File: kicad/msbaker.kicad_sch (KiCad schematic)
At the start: 32 parts

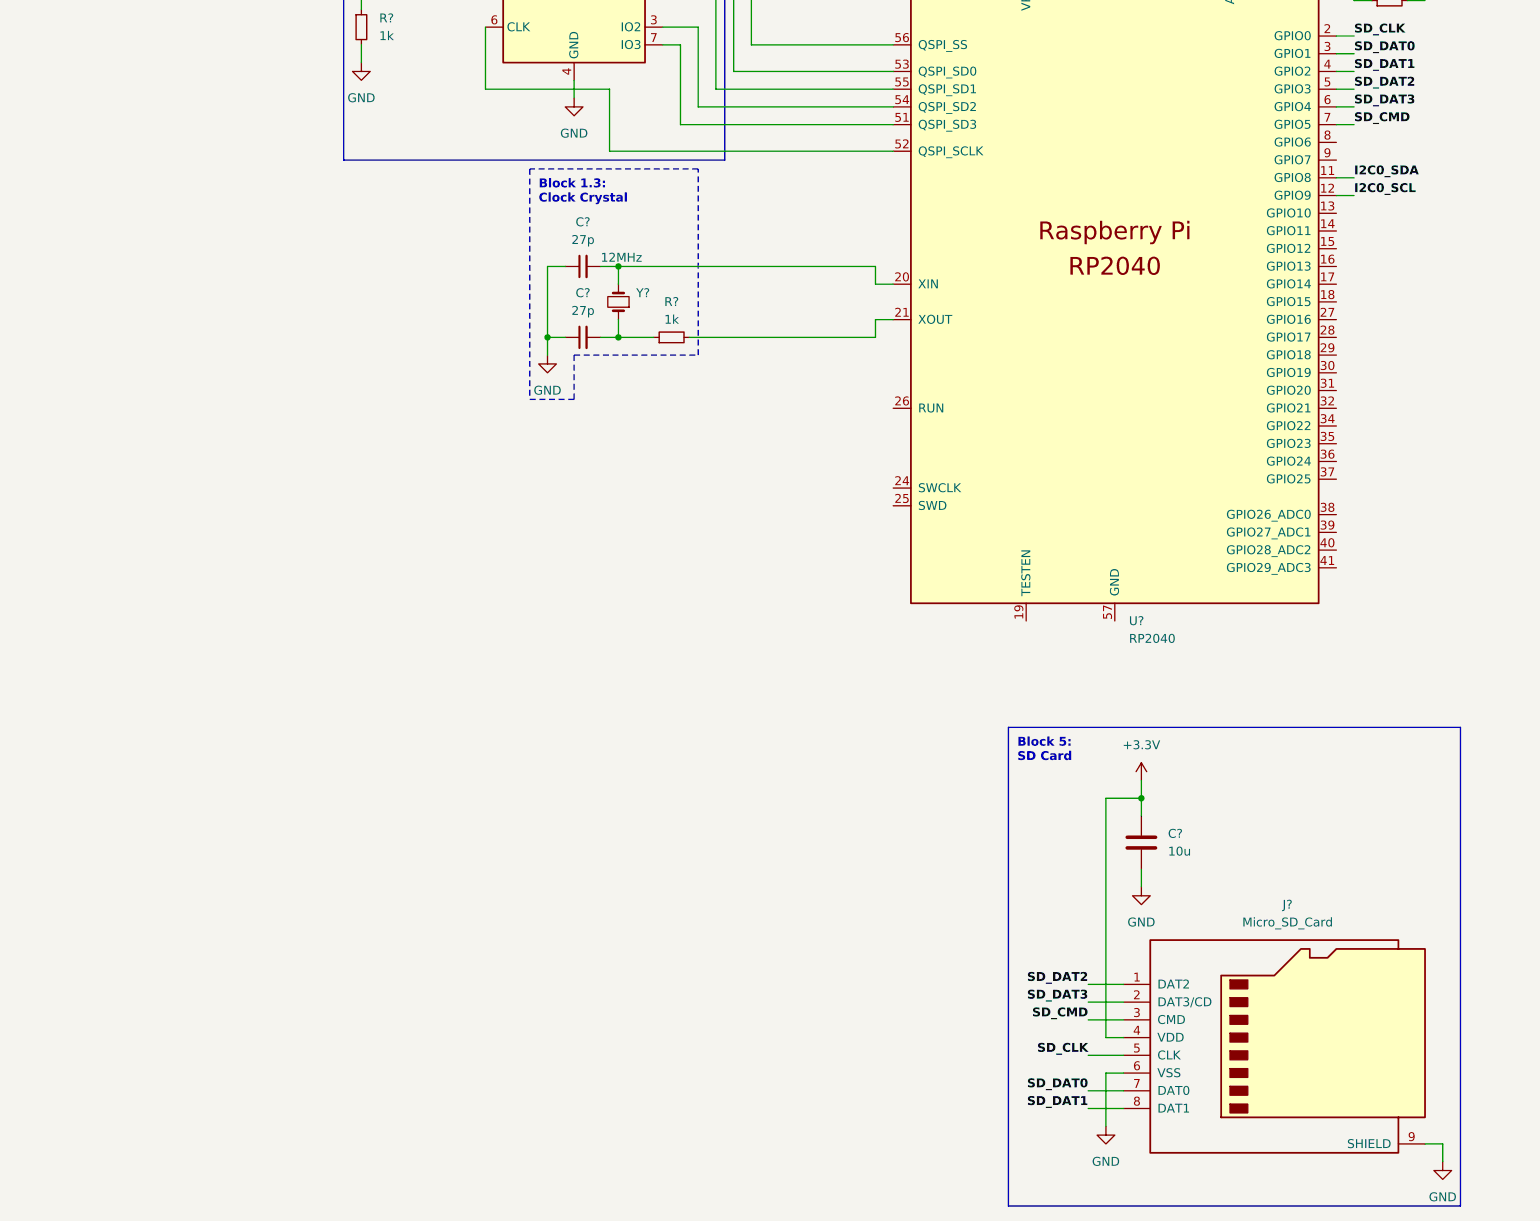
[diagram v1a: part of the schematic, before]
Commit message: Added gpio block
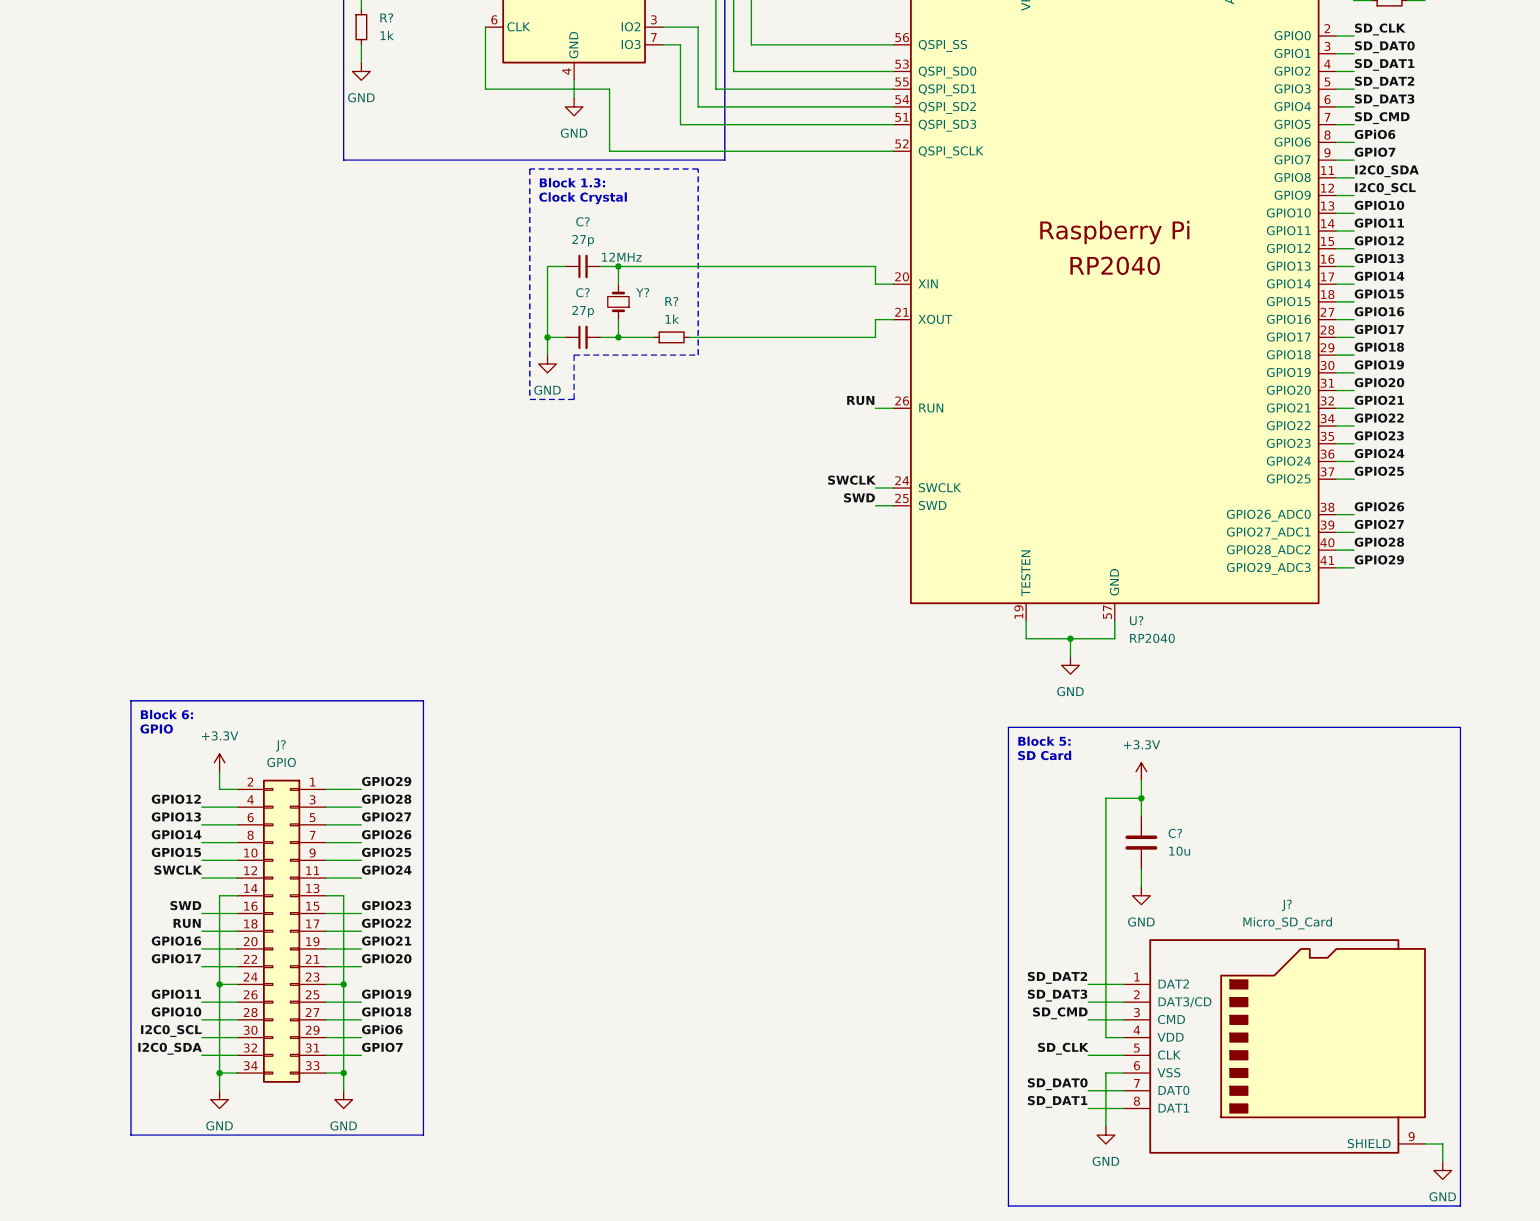
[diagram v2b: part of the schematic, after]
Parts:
- added J?: GPIO, symbol Connector_Generic:Conn_02x17_Odd_Even
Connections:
- net +3.3V: now also J?.2 (Pin_2)
- net GND: now also U?.19 (TESTEN), U?.57 (GND), J?.13 (Pin_13), J?.14 (Pin_14), J?.23 (Pin_23), J?.24 (Pin_24), J?.33 (Pin_33), J?.34 (Pin_34)
- net I2C0_SCL: now also J?.30 (Pin_30)
- net I2C0_SDA: now also J?.32 (Pin_32)
- net GPIO10: now reaches U?.13 (GPIO10)
- net GPIO10: now also J?.28 (Pin_28)
- net GPIO11: now reaches U?.14 (GPIO11)
- net GPIO11: now also J?.26 (Pin_26)
- net GPIO12: now reaches U?.15 (GPIO12)
- net GPIO12: now also J?.4 (Pin_4)
- net GPIO13: now reaches U?.16 (GPIO13)
- net GPIO13: now also J?.6 (Pin_6)
- net GPIO14: now reaches U?.17 (GPIO14)
- net GPIO14: now also J?.8 (Pin_8)
- net GPIO15: now reaches U?.18 (GPIO15)
- net GPIO15: now also J?.10 (Pin_10)
- net SWCLK: now reaches U?.24 (SWCLK)
- net SWCLK: now also J?.12 (Pin_12)
- net SWD: now reaches U?.25 (SWD)
- net SWD: now also J?.16 (Pin_16)
- net RUN: now reaches U?.26 (RUN)
- net RUN: now also J?.18 (Pin_18)
- net GPIO16: now reaches U?.27 (GPIO16)
- net GPIO16: now also J?.20 (Pin_20)
- net GPIO17: now reaches U?.28 (GPIO17)
- net GPIO17: now also J?.22 (Pin_22)
- net GPIO18: now reaches U?.29 (GPIO18)
- net GPIO18: now also J?.27 (Pin_27)
- net GPIO19: now reaches U?.30 (GPIO19)
- net GPIO19: now also J?.25 (Pin_25)
- net GPIO20: now reaches U?.31 (GPIO20)
- net GPIO20: now also J?.21 (Pin_21)
- net GPIO21: now reaches U?.32 (GPIO21)
- net GPIO21: now also J?.19 (Pin_19)
- net GPIO22: now reaches U?.34 (GPIO22)
- net GPIO22: now also J?.17 (Pin_17)
- net GPIO23: now reaches U?.35 (GPIO23)
- net GPIO23: now also J?.15 (Pin_15)
- net GPIO24: now reaches U?.36 (GPIO24)
- net GPIO24: now also J?.11 (Pin_11)
- net GPIO25: now reaches U?.37 (GPIO25)
- net GPIO25: now also J?.9 (Pin_9)
- net GPIO26: now reaches U?.38 (GPIO26_ADC0)
- net GPIO26: now also J?.7 (Pin_7)
- net GPIO27: now reaches U?.39 (GPIO27_ADC1)
- net GPIO27: now also J?.5 (Pin_5)
- net GPIO28: now reaches U?.40 (GPIO28_ADC2)
- net GPIO28: now also J?.3 (Pin_3)
- net GPIO29: now reaches U?.41 (GPIO29_ADC3)
- net GPIO29: now also J?.1 (Pin_1)
- net GPiO6: now reaches U?.8 (GPIO6)
- net GPiO6: now also J?.29 (Pin_29)
- net GPIO7: now reaches U?.9 (GPIO7)
- net GPIO7: now also J?.31 (Pin_31)
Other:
- note added: "Block 6: GPIO"

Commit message: Changed the layout of the schematic
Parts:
- added R? (x2): 15k, symbol Device:R
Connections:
- net +3.3V: now also R?.1, R?.1
- net I2C0_SDA: now also R?.2
- new net I2C_SCL: R?.2
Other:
- note added: "Block 1: MCU"
- note added: "Block 6: I2C Pullup"
- note added: "Since neither the RP2040 nor the LSM6DSO32 have thier pin capacitance in their datasheets, we will have to assume the pin capacitance each is approximately 10pf, and with a combined capacitance of 20pf we can calculate the maximum resistance to be equal to the following equation: Rp(max) = rt / ( 0.8473 * Cb ) Rp(max) = 300ns / (0.8473 * 20pF) = 17.7kOhms From there we do 80% of that resistance v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"
- moved on the sheet: C?, J?, JP?, R?, U?, Y?

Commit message: Assigned footprints
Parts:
- C1, C2, C3: renamed from C?; footprint (none) -> Capacitor_SMD:C_1206_3216Metric
- C10, C11, C12, C13, C14, C15, C16, C17, C18, C19, C20, C4, C5, C6, C7, C8, C9: renamed from C?; footprint (none) -> Capacitor_SMD:C_0402_1005Metric
- J1: renamed from J?; footprint (none) -> Connector_USB:USB_Micro-B_Molex-105017-0001
- J2: renamed from J?; footprint (none) -> Connector_Card:microSD_HC_Molex_104031-0811
- J3: renamed from J?; footprint (none) -> msbaker:5055513420
- JP1: renamed from JP?; footprint (none) -> Connector_PinHeader_2.54mm:PinHeader_1x02_P2.54mm_Vertical
- R1, R2, R3, R4, R5, R6: renamed from R?; footprint (none) -> Resistor_SMD:R_0402_1005Metric
- Y1: renamed from Y?; footprint (none) -> Crystal:Crystal_SMD_5032-2Pin_5.0x3.2mm; MPN ABLS-12.000MHZ-B4-T -> 445I23D12M00000
- gave numbers to parts that had none: 4
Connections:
- no-connect marks 4 -> 3

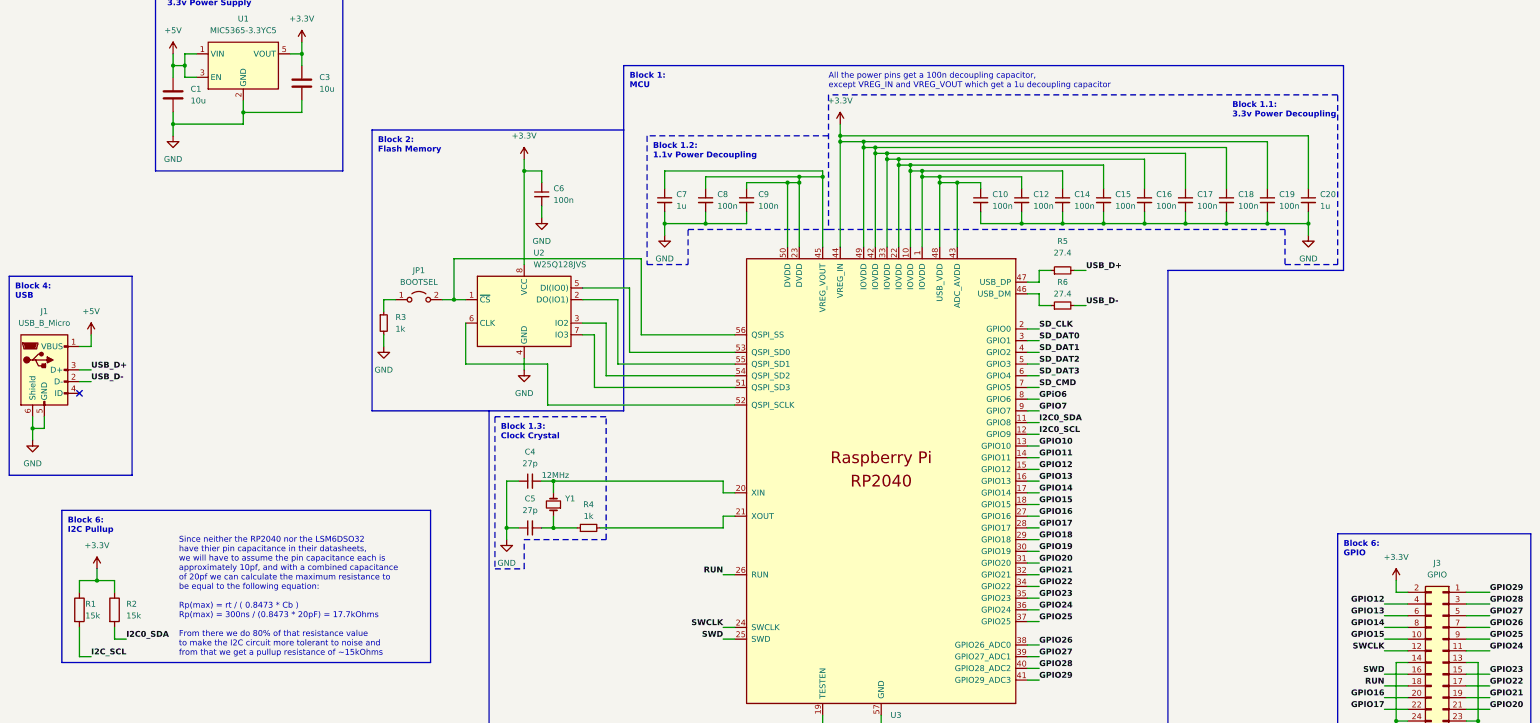
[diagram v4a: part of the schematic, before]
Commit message: Applied footprints + Added LED block + Created design checklist
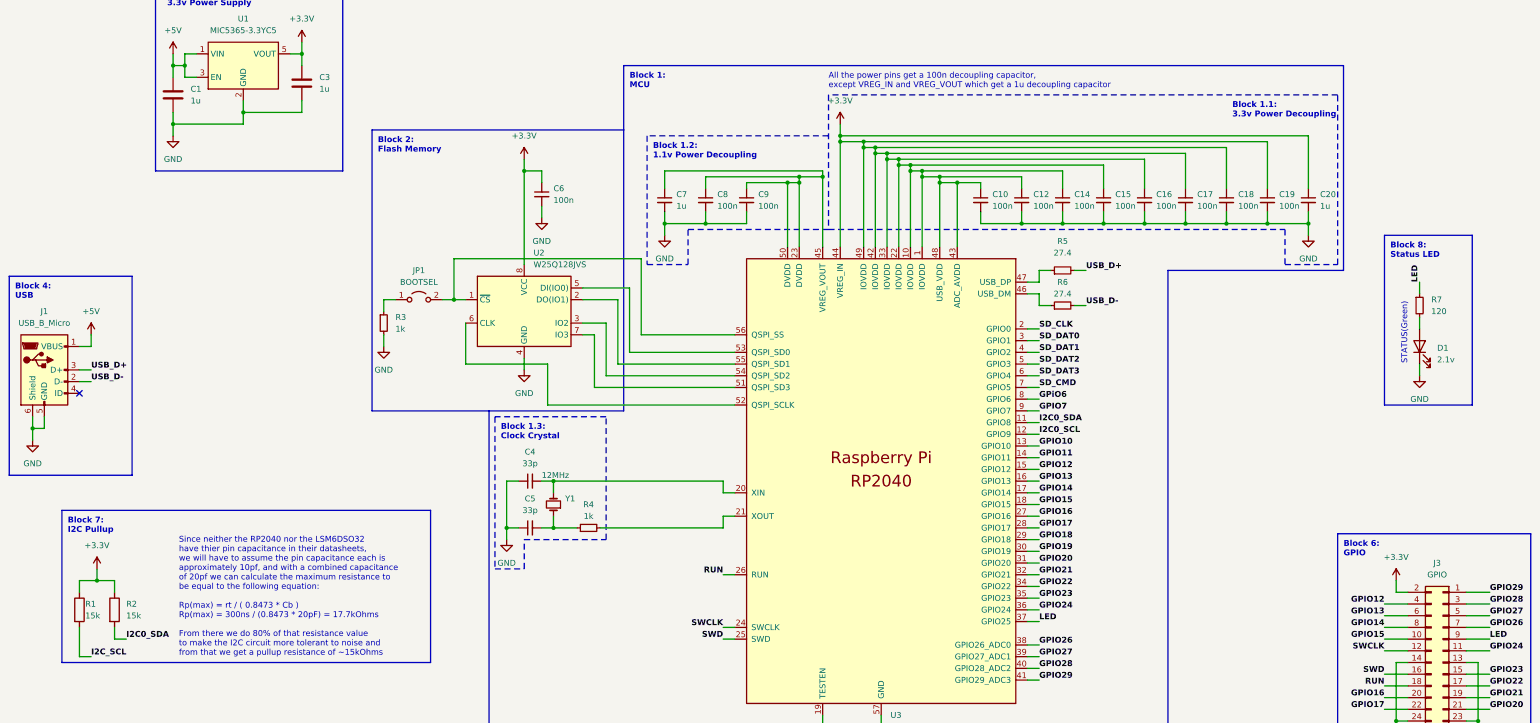
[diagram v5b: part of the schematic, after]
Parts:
- added D1: 2.1v, LED_SMD:LED_0402_1005Metric, symbol Device:LED
- added R7: 120, Resistor_SMD:R_0402_1005Metric, symbol Device:R_Small
- C1, C3: value 10u -> 1u; footprint Capacitor_SMD:C_1206_3216Metric -> Capacitor_SMD:C_0402_1005Metric; Cost (none) -> 0.19; MPN (none) -> C1005X5R1E105K050BE
- C10, C11, C12, C13, C14, C15, C16, C17, C18, C19, C6, C8, C9: Cost (none) -> 0.2; MPN (none) -> C1005X7R1H104K050BE
- C2: footprint Capacitor_SMD:C_1206_3216Metric -> Capacitor_SMD:C_0603_1608Metric; Cost (none) -> 0.38; MPN (none) -> C1608X5R0J106K080AE
- C20, C7: Cost (none) -> 0.19; MPN (none) -> C1005X5R1E105K050BE
- C4, C5: value 27p -> 33p; Cost (none) -> 0.1; MPN (none) -> CGA2B2C0G1H330J050BA
- J1: Cost (none) -> 0.96; MPN (none) -> 105017-0001
- J2: Cost (none) -> 2.22; MPN (none) -> 104031-0811
- J3: Cost (none) -> 1.57
- R1, R2: Cost (none) -> 0.1; MPN (none) -> AC0402FR-0715KL
- R3, R4: Cost (none) -> 0.1; MPN (none) -> AC0402FR-071KL
- R5, R6: Cost (none) -> 0.1; MPN (none) -> AC0402FR-0727R4L
- U1: Cost (none) -> 0.19; MPN (none) -> MIC5365-3.3YC5-TR
- U2: Cost (none) -> 1.95; MPN (none) -> W25Q128JVSIM TR
- U3: Cost (none) -> 1; MPN (none) -> RP2040TR13
- U4: Cost (none) -> 5.47; MPN (none) -> LSM6DSO32TR
- Y1: Cost (none) -> 0.76
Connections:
- net GND: now also D1.1 (K)
- net GPIO25 renamed LED
- net LED: now also R7.1
- new net: D1.2 (A), R7.2
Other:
- note added: "Block 7: I2C Pullup"
- note added: "Block 8: Status LED"
- note added: "STATUS(Green)"
- note removed: "Block 6: I2C Pullup"
